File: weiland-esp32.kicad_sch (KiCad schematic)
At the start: 38 parts, among them J1 S02B-PASK-2, J6 S02B-PASK-2, J7 S02B-PASK-2, P1 S04B-PASK-2_LF__SN_, P2 S04B-PASK-2_LF__SN_, U1 ESP32-WROOM-32E(8MB), U2 AMS1117-3.3_C347222, U3 MAX98357AETE_T, U5 ULN2003F12FN-7, U6 DZ127S-22-06-55

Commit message: latest
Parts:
- removed J6: S02B-PASK-2, footprints:CONN2_S02B-PASK-2_JST, symbol jst2pin:S02B-PASK-2
- added R3: 56kOhm, Resistor_SMD:R_0402_1005Metric, symbol 0402WGF5101TCE
- added USB1: GT-USB-7100A, easyeda2kicad:USB-C-SMD_GT-USB-7100A, symbol easyeda2kicad:GT-USB-7100A
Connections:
- net +5V: now also R3.2, USB1.A9 (VBUS), USB1.B9 (VBUS)
- net GND: now also USB1.A12 (GND), USB1.B12 (GND), USB1.EH1, USB1.EH2
- new net: R3.1, USB1.A5 (CC1)
- new net Dn: USB1.A7 (D-)
- new net Dp: USB1.A6 (D+)
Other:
- moved on the sheet: C3, J1, J7, P1, P2, U6

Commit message: test
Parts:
- removed J1, J7: S02B-PASK-2, footprints:CONN2_S02B-PASK-2_JST, symbol jst2pin:S02B-PASK-2
- removed P1, P2: S04B-PASK-2_LF__SN_, S04B-PASK-2_LF__SN_:JST_S04B-PASK-2, symbol S04B-PASK-2:S04B-PASK-2_LF__SN_
- removed USB1: GT-USB-7100A, easyeda2kicad:USB-C-SMD_GT-USB-7100A, symbol easyeda2kicad:GT-USB-7100A
- added CN1: SM05B-SRSS-TB (LF)(SN), easyeda2kicad:CONN-SMD_SM05B-SRSS-TB-LF-SN, symbol easyeda2kicad:SM05B-SRSS-TB(LF)(SN)
- added CN2, CN3: SM04B-SRSS-TB (LF)(SN), easyeda2kicad:CONN-SMD_4P-P1.00_SM04B-SRSS-TB-LF-SN, symbol easyeda2kicad:SM04B-SRSS-TB(LF)(SN)
- added CN4, CN5: SM02B-SRSS-TB (LF)(SN), easyeda2kicad:CONN-SMD_2P-P1.00_SM02B-SRSS-TB-LF-SN, symbol easyeda2kicad:SM02B-SRSS-TB(LF)(SN)
- added USB1: TYPE-C 16PIN 2MD(073), easyeda2kicad:USB-C-SMD_TYPE-C-6PIN-2MD-073, symbol easyeda2kicad:TYPE-C16PIN2MD(073)
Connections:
- net +5V: now also CN1.1, CN2.2, CN2.4, CN3.2, CN3.4, USB1.11 (VBUS), USB1.2 (VBUS)
- net Dn: now also CN1.2, USB1.5 (DN2), USB1.7 (DN1)
- net Dp: now also CN1.3, USB1.6 (DP1), USB1.8 (DP2)
- net GND: now also CN1.4, CN1.6, CN1.7, CN2.5, CN2.6, CN3.5, CN3.6, CN4.3, CN4.4, CN5.3, CN5.4, USB1.1 (GND), USB1.12 (GND), USB1.13 (SHELL), USB1.14 (SHELL)
- net OUTA: now also CN3.1
- net OUTB: now also CN3.3
- net OUTC: now also CN2.3
- net OUTD: now also CN2.1
- net OUTN: now also CN4.2, CN5.1
- net OUTP: now also CN4.1, CN5.2
- net at R3.1: now also USB1.4 (CC1)
- no-connect marks 24 -> 27
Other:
- moved on the sheet: R3, U5

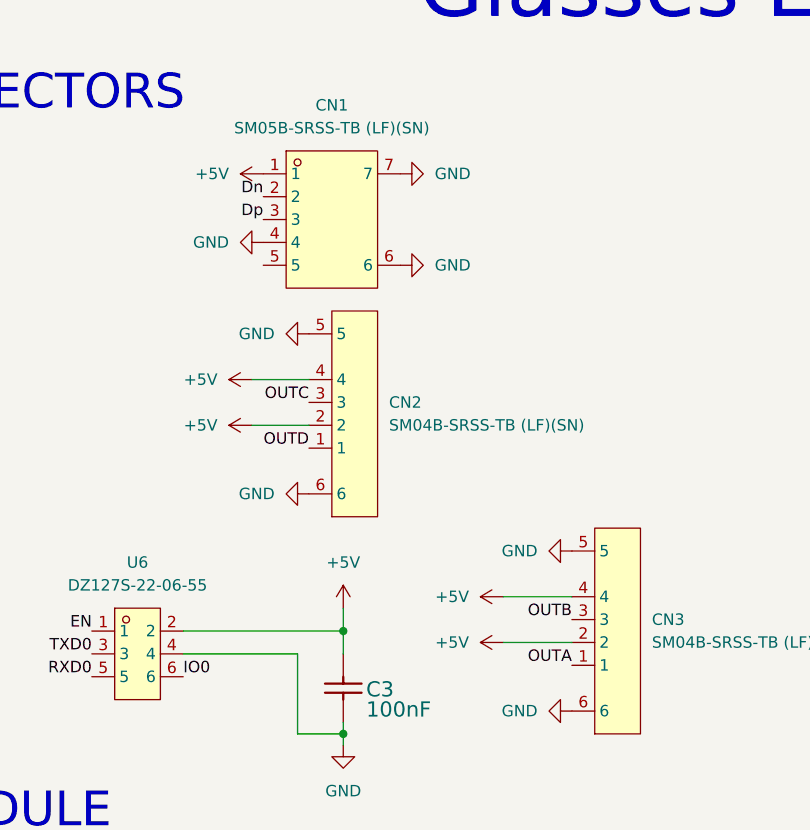
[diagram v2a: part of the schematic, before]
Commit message: working board but wrong placement of holes
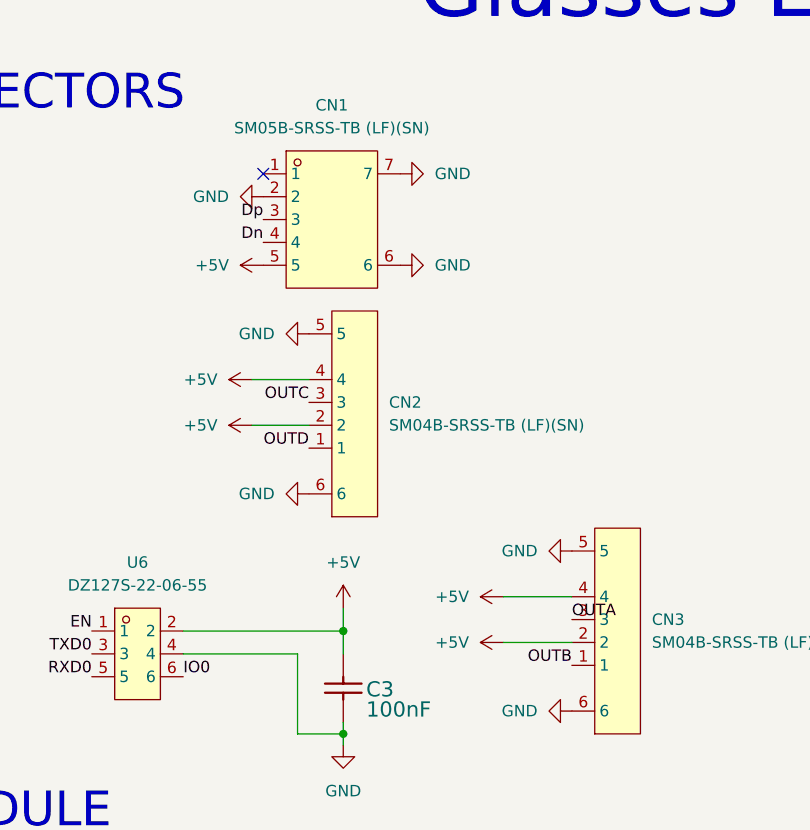
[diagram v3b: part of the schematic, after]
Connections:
- net +5V: now also CN1.5; no longer CN1.1
- net Dn: now also CN1.4; no longer CN1.2
- net GND: now also CN1.2; no longer CN1.4
- net OUTA: now also CN3.3; no longer CN3.1
- net OUTB: now also CN3.1; no longer CN3.3
- no-connect marks 27 -> 28
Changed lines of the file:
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@@
 	)
 	(no_connect
+		(at 95.25 35.56)
+	)
+	(no_connect
 		(at 96.52 171.45)
 	)
@@
 		)
 	)
-	(label "OUTB"
-		(at 129.54 85.09 180)
-		(fields_autoplaced yes)
-		(effects
-			(font
-				(size 1.27 1.27)
-			)
-			(justify right bottom)
-		)
-	)
 	(label "OUTD"
 		(at 215.9 64.77 0)
@@
 		)
 	)
-	(label "OUTA"
-		(at 129.54 90.17 180)
-		(fields_autoplaced yes)
-		(effects
-			(font
-				(size 1.27 1.27)
-			)
-			(justify right bottom)
-		)
-	)
 	(label "OUTN"
 		(at 21.59 82.55 180)
@@
 		)
 	)
-	(label "Dn"
-		(at 95.25 38.1 180)
-		(fields_autoplaced yes)
-		(effects
-			(font
-				(size 1.27 1.27)
-			)
-			(justify right bottom)
-		)
-	)
 	(label "IO15"
 		(at 339.09 151.13 270)
@@
 		)
 	)
+	(label "OUTA"
+		(at 129.54 85.09 0)
+		(fields_autoplaced yes)
+		(effects
+			(font
+				(size 1.27 1.27)
+			)
+			(justify left bottom)
+		)
+	)
 	(label "OUTP"
 		(at 21.59 80.01 180)
@@
 		)
 	)
+	(label "OUTB"
+		(at 129.54 90.17 180)
+		(fields_autoplaced yes)
+		(effects
+			(font
+				(size 1.27 1.27)
+			)
+			(justify right bottom)
+		)
+	)
 	(label "IO17"
 		(at 368.3 138.43 270)
@@
 		)
 	)
+	(label "Dn"
+		(at 95.25 43.18 180)
+		(fields_autoplaced yes)
+		(effects
+			(font
+				(size 1.27 1.27)
+			)
+			(justify right bottom)
+		)
+	)
 	(label "OUTN"
 		(at 317.5 92.71 180)
@@
 	(symbol
 		(lib_id "power:+5V")
-		(at 95.25 35.56 90)
-		(unit 1)
-		(exclude_from_sim no)
-		(in_bom yes)
-		(on_board yes)
-		(dnp no)
-		(fields_autoplaced yes)
-		(property "Reference" "#PWR06"
-			(at 99.06 35.56 0)
-			(effects
-				(font
-					(size 1.27 1.27)
-				)
-				(hide yes)
-			)
-		)
-		(property "Value" "+5V"
-			(at 91.44 35.5599 90)
-			(effects
-				(font
-					(size 1.27 1.27)
-				)
-				(justify left)
-			)
-		)
-		(property "Footprint" ""
-			(at 95.25 35.56 0)
-			(effects
-				(font
-					(size 1.27 1.27)
-				)
-				(hide yes)
-			)
-		)
-		(property "Datasheet" ""
-			(at 95.25 35.56 0)
-			(effects
-				(font
-					(size 1.27 1.27)
-				)
-				(hide yes)
-			)
-		)
-		(property "Description" "Power symbol creates a global label with name \"+5V\""
-			(at 95.25 35.56 0)
-			(effects
-				(font
-					(size 1.27 1.27)
-				)
-				(hide yes)
-			)
-		)
-		(pin "1"
-		)
-		(instances
-			(project "weiland-esp32"
-				(path "/745a8d65-fa51-45f7-9665-7610e72f2a80"
-					(reference "#PWR06")
-					(unit 1)
-				)
-			)
-		)
-	)
-	(symbol
-		(lib_id "power:+5V")
 		(at 163.83 149.86 0)
 		(unit 1)
@@
 	(symbol
 		(lib_id "power:GND")
-		(at 95.25 43.18 270)
-		(unit 1)
-		(exclude_from_sim no)
-		(in_bom yes)
-		(on_board yes)
-		(dnp no)
-		(fields_autoplaced yes)
-		(property "Reference" "#PWR031"
-			(at 88.9 43.18 0)
-			(effects
-				(font
-					(size 1.27 1.27)
-				)
-				(hide yes)
-			)
-		)
-		(property "Value" "GND"
-			(at 91.44 43.1799 90)
-			(effects
-				(font
-					(size 1.27 1.27)
-				)
-				(justify right)
-			)
-		)
-		(property "Footprint" ""
-			(at 95.25 43.18 0)
-			(effects
-				(font
-					(size 1.27 1.27)
-				)
-				(hide yes)
-			)
-		)
-		(property "Datasheet" ""
-			(at 95.25 43.18 0)
-			(effects
-				(font
-					(size 1.27 1.27)
-				)
-				(hide yes)
-			)
-		)
-		(property "Description" "Power symbol creates a global label with name \"GND\" , ground"
-			(at 95.25 43.18 0)
-			(effects
-				(font
-					(size 1.27 1.27)
-				)
-				(hide yes)
-			)
-		)
-		(pin "1"
-		)
-		(instances
-			(project "weiland-esp32"
-				(path "/745a8d65-fa51-45f7-9665-7610e72f2a80"
-					(reference "#PWR031")
-					(unit 1)
-				)
-			)
-		)
-	)
-	(symbol
-		(lib_id "power:GND")
 		(at 27.94 140.97 0)
 		(unit 1)
@@
 	(symbol
 		(lib_id "power:GND")
+		(at 95.25 38.1 270)
+		(unit 1)
+		(exclude_from_sim no)
+		(in_bom yes)
+		(on_board yes)
+		(dnp no)
+		(fields_autoplaced yes)
+		(property "Reference" "#PWR031"
+			(at 88.9 38.1 0)
+			(effects
+				(font
+					(size 1.27 1.27)
+				)
+				(hide yes)
+			)
+		)
+		(property "Value" "GND"
+			(at 91.44 38.0999 90)
+			(effects
+				(font
+					(size 1.27 1.27)
+				)
+				(justify right)
+			)
+		)
+		(property "Footprint" ""
+			(at 95.25 38.1 0)
+			(effects
+				(font
+					(size 1.27 1.27)
+				)
+				(hide yes)
+			)
+		)
+		(property "Datasheet" ""
+			(at 95.25 38.1 0)
+			(effects
+				(font
+					(size 1.27 1.27)
+				)
+				(hide yes)
+			)
+		)
+		(property "Description" "Power symbol creates a global label with name \"GND\" , ground"
+			(at 95.25 38.1 0)
+			(effects
+				(font
+					(size 1.27 1.27)
+				)
+				(hide yes)
+			)
+		)
+		(pin "1"
+		)
+		(instances
+			(project "weiland-esp32"
+				(path "/745a8d65-fa51-45f7-9665-7610e72f2a80"
+					(reference "#PWR031")
+					(unit 1)
+				)
+			)
+		)
+	)
+	(symbol
+		(lib_id "power:GND")
 		(at 199.39 167.64 0)
 		(unit 1)
@@
 					(unit 1)
 				)
+			)
+		)
+	)
+	(symbol
+		(lib_id "power:+5V")
+		(at 95.25 45.72 90)
+		(unit 1)
+		(exclude_from_sim no)
+		(in_bom yes)
+		(on_board yes)
+		(dnp no)
+		(fields_autoplaced yes)
+		(property "Reference" "#PWR06"
+			(at 99.06 45.72 0)
+			(effects
+				(font
+					(size 1.27 1.27)
+				)
+				(hide yes)
+			)
+		)
+		(property "Value" "+5V"
+			(at 91.44 45.7199 90)
+			(effects
+				(font
+					(size 1.27 1.27)
+				)
+				(justify left)
+			)
+		)
+		(property "Footprint" ""
+			(at 95.25 45.72 0)
+			(effects
+				(font
+					(size 1.27 1.27)
+				)
+				(hide yes)
+			)
+		)
+		(property "Datasheet" ""
+			(at 95.25 45.72 0)
+			(effects
+				(font
+					(size 1.27 1.27)
+				)
+				(hide yes)
+			)
+		)
+		(property "Description" "Power symbol creates a global label with name \"+5V\""
+			(at 95.25 45.72 0)
+			(effects
+				(font
+					(size 1.27 1.27)
+				)
+				(hide yes)
+			)
+		)
+		(pin "1"
+		)
+		(instances
+			(project "weiland-esp32"
+				(path "/745a8d65-fa51-45f7-9665-7610e72f2a80"
+					(reference "#PWR06")
+					(unit 1)
+				)
